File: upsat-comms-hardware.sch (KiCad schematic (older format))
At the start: 195 parts, among them J1 SMA, J2 SMA, P1 SWD, P2 OBC, P3 CONN_02X03, U1 TXCO_TG_5021CG, U10 CC1120, U12 ADT7420, U14 OPA320, U16 RF5110G, U18 FA_128_, U2 TPS79930, U3 FA_128_, U4 CC1120, U5 STM32F407VG, U6 TXCO_TG_5021CG, U8 TPS79930, Y1 Crystal, Y2 Crystal

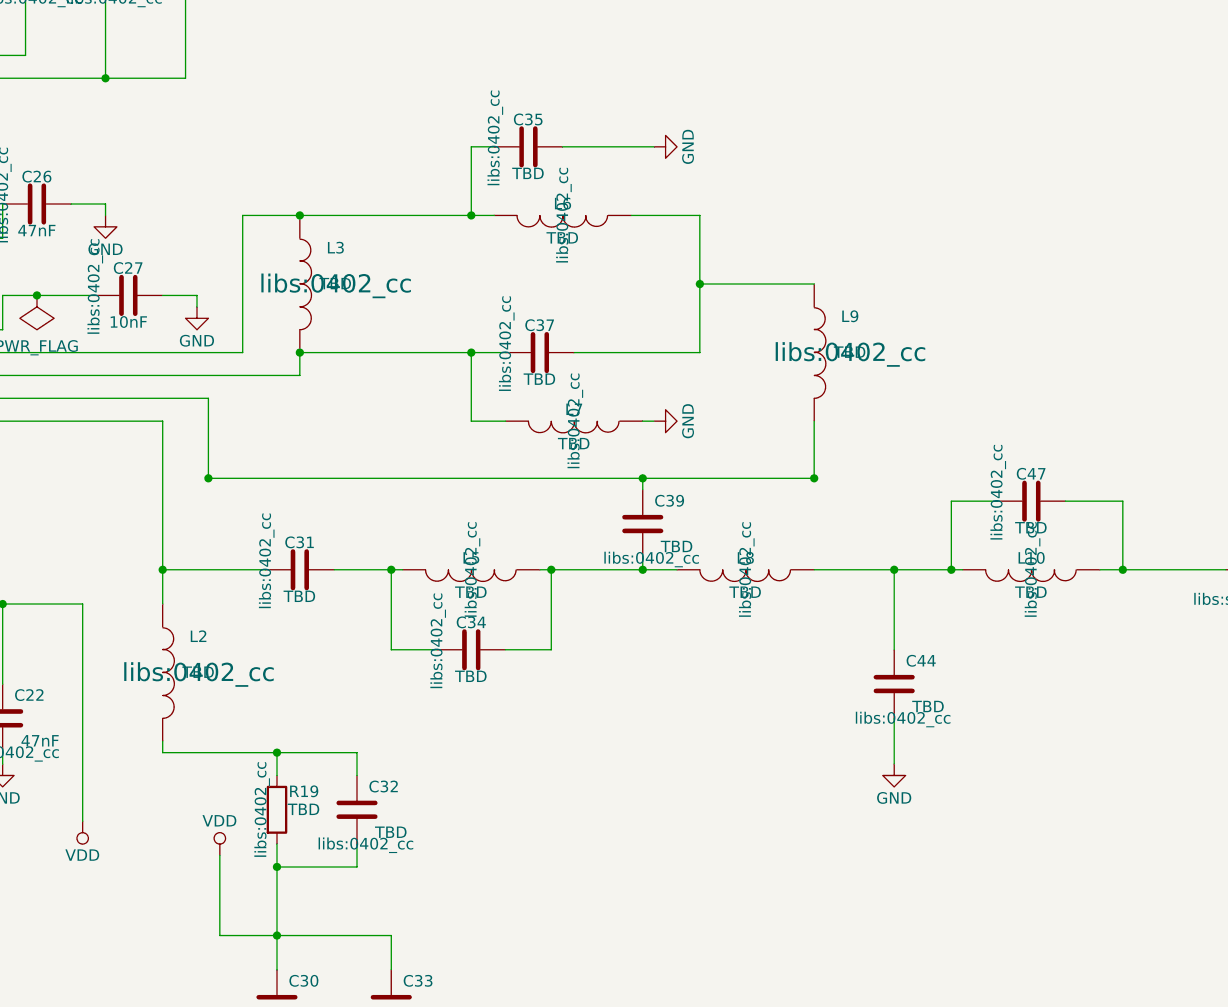
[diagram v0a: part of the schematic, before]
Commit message: add RF values for CC1120 RX, wrong path for mmcx con.
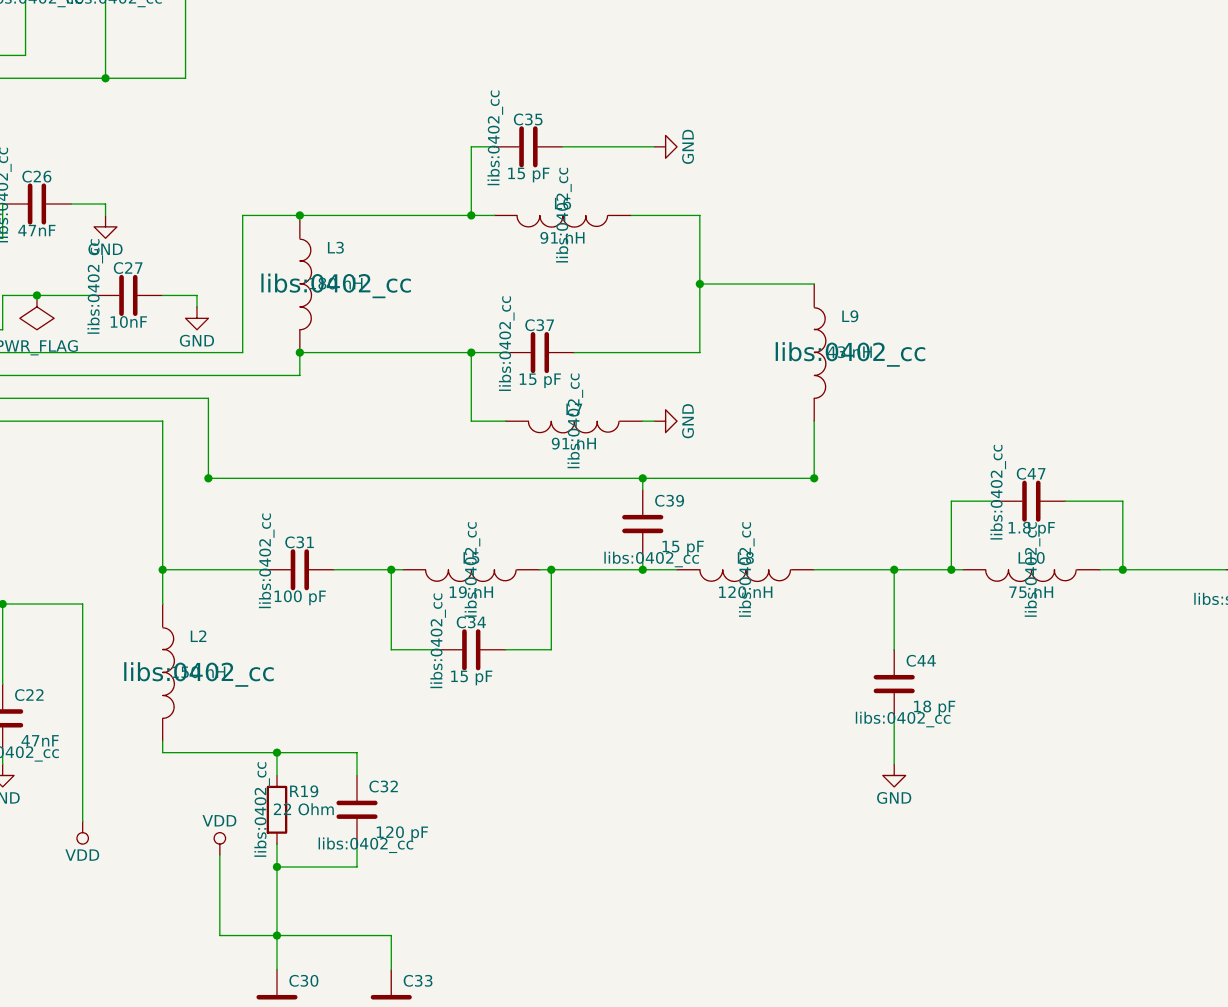
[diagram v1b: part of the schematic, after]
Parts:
- C31: value TBD -> 100 pF
- C32: value TBD -> 120 pF
- C34, C35, C37, C39: value TBD -> 15 pF
- C44: value TBD -> 18 pF
- C47: value TBD -> 1.8 pF
- L10: value TBD -> 75 nH
- L2: value TBD -> 150 nH
- L3: value TBD -> 180 nH
- L5: value TBD -> 19 nH
- L6, L7: value TBD -> 91 nH
- L8: value TBD -> 120 nH
- L9: value TBD -> 43 nH
- R19: value TBD -> 22 Ohm
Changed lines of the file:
@@
 P 6350 16800
 F 0 "L2" H 6507 16957 50  0000 C CNN
-F 1 "TBD" H 6507 16800 50  0000 C CNN
+F 1 "150 nH" H 6507 16800 50  0000 C CNN
 F 2 "libs:0402_cc" H 6507 16800 79  0000 C CNN
 F 3 "" H 6350 16800 50  0000 C CNN
@@
 P 6850 17400
 F 0 "R19" H 6968 17479 50  0000 C CNN
-F 1 "TBD" H 6968 17400 50  0000 C CNN
+F 1 "22 Ohm" H 6968 17400 50  0000 C CNN
 F 2 "libs:0402_cc" V 6780 17400 50  0000 C CNN
 F 3 "" H 6850 17400 50  0000 C CNN
@@
 P 7200 17400
 F 0 "C32" H 7318 17500 50  0000 C CNN
-F 1 "TBD" H 7279 17300 50  0000 L CNN
+F 1 "120 pF" H 7279 17300 50  0000 L CNN
 F 2 "libs:0402_cc" H 7238 17250 50  0000 C CNN
 F 3 "" H 7200 17400 50  0000 C CNN
@@
 P 6950 16350
 F 0 "C31" V 7068 16350 50  0000 C CNN
-F 1 "TBD" V 6832 16350 50  0000 C CNN
+F 1 "100 pF" V 6832 16350 50  0000 C CNN
 F 2 "libs:0402_cc" H 6988 16200 50  0000 C CNN
 F 3 "" H 6950 16350 50  0000 C CNN
@@
 P 7700 16350
 F 0 "L5" V 7650 16350 50  0000 C CNN
-F 1 "TBD" V 7800 16350 50  0000 C CNN
+F 1 "19 nH" V 7800 16350 50  0000 C CNN
 F 2 "libs:0402_cc" H 7700 16350 50  0000 C CNN
 F 3 "" H 7700 16350 50  0000 C CNN
@@
 P 7700 16700
 F 0 "C34" V 7818 16700 50  0000 C CNN
-F 1 "TBD" V 7582 16700 50  0000 C CNN
+F 1 "15 pF" V 7582 16700 50  0000 C CNN
 F 2 "libs:0402_cc" H 7738 16550 50  0000 C CNN
 F 3 "" H 7700 16700 50  0000 C CNN
@@
 P 8450 16150
 F 0 "C39" H 8568 16250 50  0000 C CNN
-F 1 "TBD" H 8529 16050 50  0000 L CNN
+F 1 "15 pF" H 8529 16050 50  0000 L CNN
 F 2 "libs:0402_cc" H 8488 16000 50  0000 C CNN
 F 3 "" H 8450 16150 50  0000 C CNN
@@
 P 6950 15100
 F 0 "L3" H 7107 15257 50  0000 C CNN
-F 1 "TBD" H 7107 15100 50  0000 C CNN
+F 1 "180 nH" H 7107 15100 50  0000 C CNN
 F 2 "libs:0402_cc" H 7107 15100 79  0000 C CNN
 F 3 "" H 6950 15100 50  0000 C CNN
@@
 P 8150 15700
 F 0 "L7" V 8100 15700 50  0000 C CNN
-F 1 "TBD" V 8250 15700 50  0000 C CNN
+F 1 "91 nH" V 8250 15700 50  0000 C CNN
 F 2 "libs:0402_cc" H 8150 15700 50  0000 C CNN
 F 3 "" H 8150 15700 50  0000 C CNN
@@
 P 8100 14800
 F 0 "L6" V 8050 14800 50  0000 C CNN
-F 1 "TBD" V 8200 14800 50  0000 C CNN
+F 1 "91 nH" V 8200 14800 50  0000 C CNN
 F 2 "libs:0402_cc" H 8100 14800 50  0000 C CNN
 F 3 "" H 8100 14800 50  0000 C CNN
@@
 P 8000 15400
 F 0 "C37" V 8118 15400 50  0000 C CNN
-F 1 "TBD" V 7882 15400 50  0000 C CNN
+F 1 "15 pF" V 7882 15400 50  0000 C CNN
 F 2 "libs:0402_cc" H 8038 15250 50  0000 C CNN
 F 3 "" H 8000 15400 50  0000 C CNN
@@
 P 7950 14500
 F 0 "C35" V 8068 14500 50  0000 C CNN
-F 1 "TBD" V 7832 14500 50  0000 C CNN
+F 1 "15 pF" V 7832 14500 50  0000 C CNN
 F 2 "libs:0402_cc" H 7988 14350 50  0000 C CNN
 F 3 "" H 7950 14500 50  0000 C CNN
@@
 P 9200 15400
 F 0 "L9" H 9357 15557 50  0000 C CNN
-F 1 "TBD" H 9357 15400 50  0000 C CNN
+F 1 "43 nH" H 9357 15400 50  0000 C CNN
 F 2 "libs:0402_cc" H 9357 15400 79  0000 C CNN
 F 3 "" H 9200 15400 50  0000 C CNN
@@
 P 8900 16350
 F 0 "L8" V 8850 16350 50  0000 C CNN
-F 1 "TBD" V 9000 16350 50  0000 C CNN
+F 1 "120 nH" V 9000 16350 50  0000 C CNN
 F 2 "libs:0402_cc" H 8900 16350 50  0000 C CNN
 F 3 "" H 8900 16350 50  0000 C CNN
@@
 P 9550 16850
 F 0 "C44" H 9668 16950 50  0000 C CNN
-F 1 "TBD" H 9629 16750 50  0000 L CNN
+F 1 "18 pF" H 9629 16750 50  0000 L CNN
 F 2 "libs:0402_cc" H 9588 16700 50  0000 C CNN
 F 3 "" H 9550 16850 50  0000 C CNN
@@
 P 10150 16350
 F 0 "L10" V 10100 16350 50  0000 C CNN
-F 1 "TBD" V 10250 16350 50  0000 C CNN
+F 1 "75 nH" V 10250 16350 50  0000 C CNN
 F 2 "libs:0402_cc" H 10150 16350 50  0000 C CNN
 F 3 "" H 10150 16350 50  0000 C CNN
@@
 P 10150 16050
 F 0 "C47" V 10268 16050 50  0000 C CNN
-F 1 "TBD" V 10032 16050 50  0000 C CNN
+F 1 "1.8 pF" V 10032 16050 50  0000 C CNN
 F 2 "libs:0402_cc" H 10188 15900 50  0000 C CNN
 F 3 "" H 10150 16050 50  0000 C CNN

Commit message: add power amp RF out component values, add comments on CC1120 TXCO-Crystal section, add comments on CC1120 regulator-bead
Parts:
- C160: value 22-30pF -> 22 pF
- C31: value 100 pF -> 150 pF
- C32: value 120 pF -> 100 pF
- L33: value 2.7-3.9nH -> 2.7 nH
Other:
- note added: "CC1120/25 uning XTAL: do not mount: U1, C3, C9, R9, R6\nCC1120/25 using TCXO: do not mount: R10, R9, C10, U3, C11: mount 0 Ohm resisitor\n X1: CC1120:32MHz and CC1125:40MHz\n R10 is a 0ohms shunt resistor that ground\n the EXT_XOSC pin when TCXO is not mounted.\n"
- note added: "CC1120/25 uning XTAL: do not mount: U6, C53, C65, R26, R24\nCC1120/25 using TCXO: do not mount: R27, R26, C67, U18, C69: mount 0 Ohm resistor\n X1: CC1120:32MHz and CC1125:40MHz\n R27 is a 0ohms shunt resistor that ground\n the EXT_XOSC pin when TCXO is not mounted.\n"
- note added: "L1 is a Bead to be mounted if the regulator U2 is not mounted,\nCC1120 ref des will default not use regulator\nCC1120/CC1125: do not mount: U2, C4, C8, C13\nTG5021CG is optional: do not mount L1 if regulator is mounted\n"
- note added: "L11 is a Bead to be mounted if the regulator U8 is not mounted,\nCC1120 ref des will default not use regulator\nCC1120/CC1125: do not mount: U8, C55, C62, C73\nTG5021CG is optional: do not mount L1 if regulator is mounted\n"
- note removed: "CC1120/25 uning XTAL: do not mount: X2, C321, C322, R321, R322\nCC1120/25 using TCXO: do not mount: R12, R321, C311, X1. C301: mount 0 Ohm resisitor\n X1: CC1120:32MHz and CC1125:40MHz\n R12 is a 0ohms shunt resistor that ground\n the EXT_XOSC pin when TCXO is not mounted.\n"
- note removed: "L1 is a Bead to be mounted if the regulator U2 is not mounted,\nCC1120 ref des will default not use regulator\nCC1120/CC1125: do not mount: U2, C12, C41, C53\nTG5021CG is optional: do not mount L1 if regulator is mounted\n"
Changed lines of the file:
@@
 $EndComp
 Text Notes 1600 18350 0    60   ~ 0
-L1 is a Bead to be mounted if the regulator U2 is not mounted,\nCC1120 ref des will default not use regulator\nCC1120/CC1125: do not mount: U2, C12, C41, C53\nTG5021CG is optional: do not mount L1 if regulator is mounted\n
+L1 is a Bead to be mounted if the regulator U2 is not mounted,\nCC1120 ref des will default not use regulator\nCC1120/CC1125: do not mount: U2, C4, C8, C13\nTG5021CG is optional: do not mount L1 if regulator is mounted\n
 $Comp
 L R R17
@@
 P 7200 17400
 F 0 "C32" H 7318 17500 50  0000 C CNN
-F 1 "120 pF" H 7279 17300 50  0000 L CNN
+F 1 "100 pF" H 7279 17300 50  0000 L CNN
 F 2 "libs:0402_cc" H 7238 17250 50  0000 C CNN
 F 3 "" H 7200 17400 50  0000 C CNN
@@
 P 6950 16350
 F 0 "C31" V 7068 16350 50  0000 C CNN
-F 1 "100 pF" V 6832 16350 50  0000 C CNN
+F 1 "150 pF" V 6832 16350 50  0000 C CNN
 F 2 "libs:0402_cc" H 6988 16200 50  0000 C CNN
 F 3 "" H 6950 16350 50  0000 C CNN
@@
 $EndComp
 Text Notes 1600 12150 0    60   ~ 0
-CC1120/25 uning XTAL: do not mount: X2, C321, C322, R321, R322\nCC1120/25 using TCXO: do not mount: R12, R321, C311, X1. C301: mount 0 Ohm resisitor\n X1: CC1120:32MHz and CC1125:40MHz\n R12 is a 0ohms shunt resistor that ground\n the EXT_XOSC pin when TCXO is not mounted.\n
+CC1120/25 uning XTAL: do not mount: U1, C3, C9, R9, R6\nCC1120/25 using TCXO: do not mount: R10, R9, C10, U3, C11: mount 0 Ohm resisitor\n X1: CC1120:32MHz and CC1125:40MHz\n R10 is a 0ohms shunt resistor that ground\n the EXT_XOSC pin when TCXO is not mounted.\n
 $Comp
 L SMA J1
@@
 P 28300 16150
 F 0 "L33" V 28250 16150 50  0000 C CNN
-F 1 "2.7-3.9nH" V 28400 16150 50  0000 C CNN
+F 1 "2.7 nH" V 28400 16150 50  0000 C CNN
 F 2 "libs:0603murata2" H 28300 16150 50  0000 C CNN
 F 3 "" H 28300 16150 50  0000 C CNN
@@
 P 28900 16550
 F 0 "C160" H 29018 16650 50  0000 C CNN
-F 1 "22-30pF" H 28979 16450 50  0000 L CNN
+F 1 "22 pF" H 28979 16450 50  0000 L CNN
 F 2 "libs:0603murata2" H 28938 16400 50  0000 C CNN
 F 3 "" H 28900 16550 50  0000 C CNN
@@
 $EndComp
 Text Notes 14350 12050 0    60   ~ 0
-CC1120/25 uning XTAL: do not mount: X2, C321, C322, R321, R322\nCC1120/25 using TCXO: do not mount: R12, R321, C311, X1. C301: mount 0 Ohm resisitor\n X1: CC1120:32MHz and CC1125:40MHz\n R12 is a 0ohms shunt resistor that ground\n the EXT_XOSC pin when TCXO is not mounted.\n
+CC1120/25 uning XTAL: do not mount: U6, C53, C65, R26, R24\nCC1120/25 using TCXO: do not mount: R27, R26, C67, U18, C69: mount 0 Ohm resistor\n X1: CC1120:32MHz and CC1125:40MHz\n R27 is a 0ohms shunt resistor that ground\n the EXT_XOSC pin when TCXO is not mounted.\n
 $Comp
 L C C139
@@
 $EndComp
 Text Notes 14350 18250 0    60   ~ 0
-L1 is a Bead to be mounted if the regulator U2 is not mounted,\nCC1120 ref des will default not use regulator\nCC1120/CC1125: do not mount: U2, C12, C41, C53\nTG5021CG is optional: do not mount L1 if regulator is mounted\n
+L11 is a Bead to be mounted if the regulator U8 is not mounted,\nCC1120 ref des will default not use regulator\nCC1120/CC1125: do not mount: U8, C55, C62, C73\nTG5021CG is optional: do not mount L1 if regulator is mounted\n
 $Comp
 L +3.3V #PWR0118

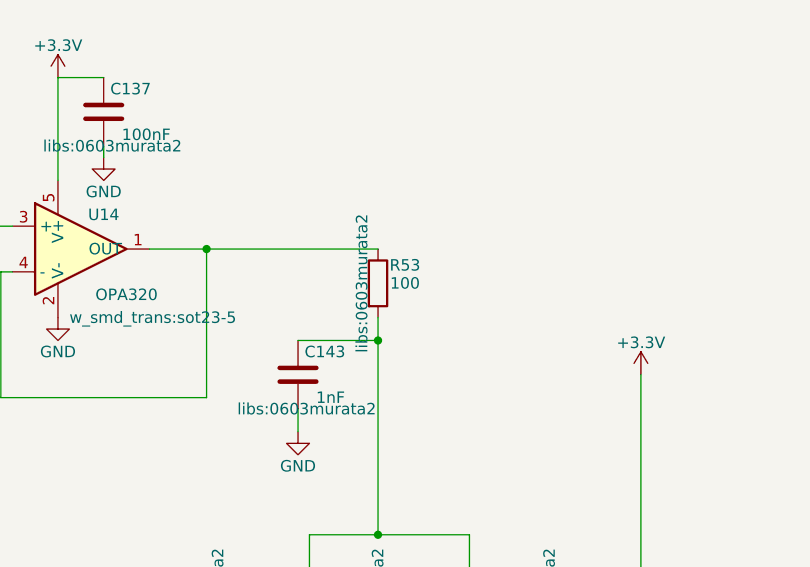
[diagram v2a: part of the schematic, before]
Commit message: Edit OPA R53 resistor
It should be 180 Ohms to feed P.A AGC with 2.75 Volts.
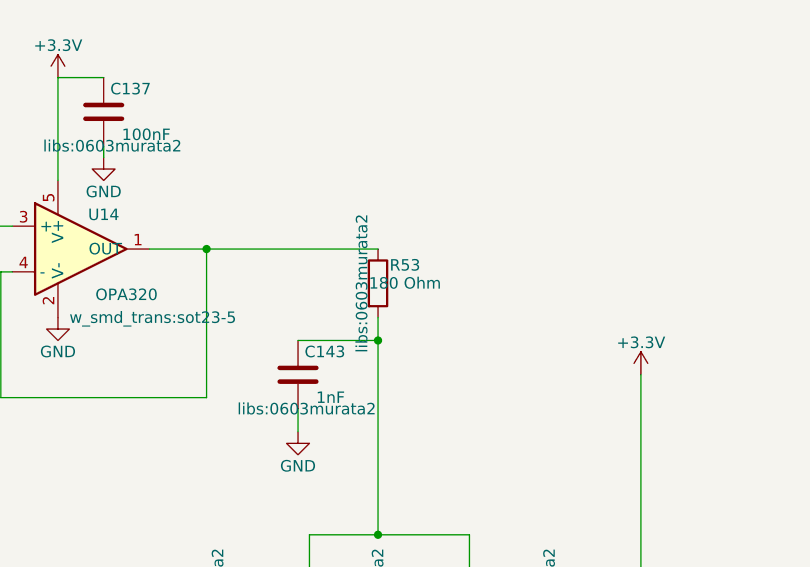
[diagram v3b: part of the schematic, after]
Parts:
- R53: value 100 -> 180 Ohm
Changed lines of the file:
@@
 P 26200 13350
 F 0 "R53" H 26318 13429 50  0000 C CNN
-F 1 "100" H 26318 13350 50  0000 C CNN
+F 1 "180 Ohm" H 26318 13350 50  0000 C CNN
 F 2 "libs:0603murata2" V 26130 13350 50  0000 C CNN
 F 3 "" H 26200 13350 50  0000 C CNN

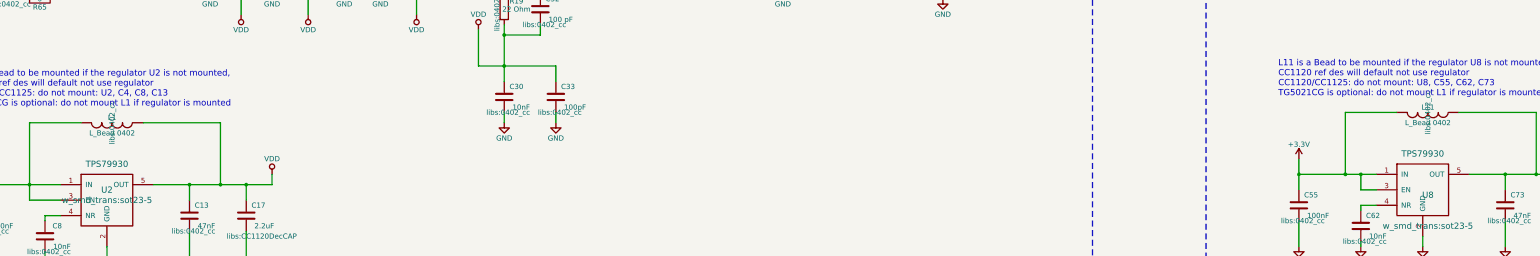
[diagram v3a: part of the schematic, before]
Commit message: Add CC1120 bead part number
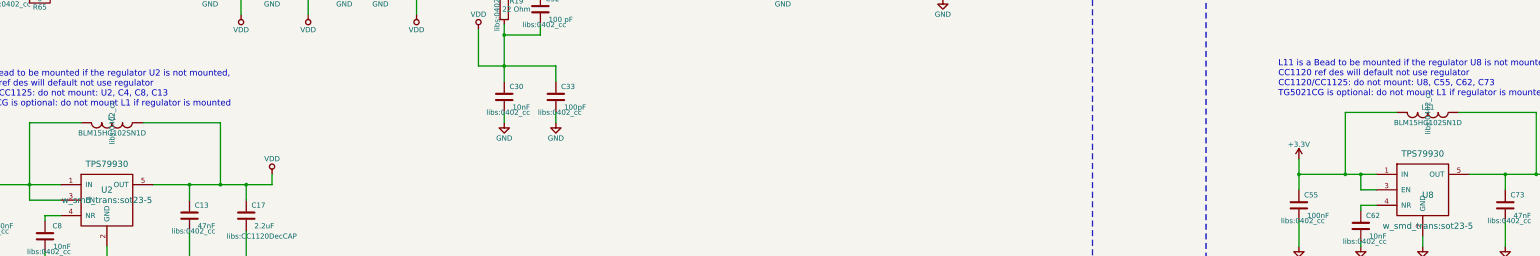
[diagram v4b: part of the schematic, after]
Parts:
- L1, L11: value L_Bead 0402 -> BLM15HG102SN1D
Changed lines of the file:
@@
 P 3050 18500
 F 0 "L1" V 3000 18500 50  0000 C CNN
-F 1 "L_Bead 0402" V 3150 18500 50  0000 C CNN
+F 1 "BLM15HG102SN1D" V 3150 18500 50  0000 C CNN
 F 2 "libs:0402_cc" H 3050 18500 50  0000 C CNN
 F 3 "" H 3050 18500 50  0000 C CNN
@@
 P 15800 18400
 F 0 "L11" V 15750 18400 50  0000 C CNN
-F 1 "L_Bead 0402" V 15900 18400 50  0000 C CNN
+F 1 "BLM15HG102SN1D" V 15900 18400 50  0000 C CNN
 F 2 "libs:0402_cc" H 15800 18400 50  0000 C CNN
 F 3 "" H 15800 18400 50  0000 C CNN

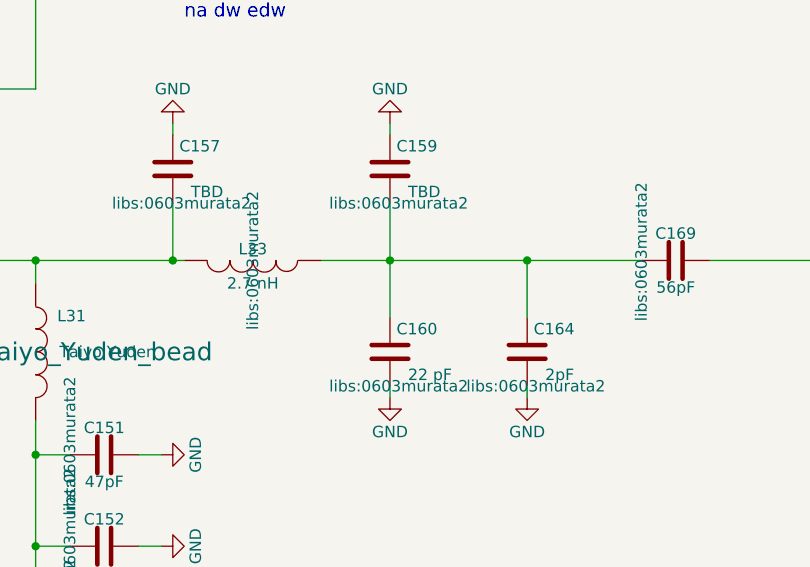
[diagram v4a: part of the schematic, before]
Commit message: Add values for P.A RF Out matching network
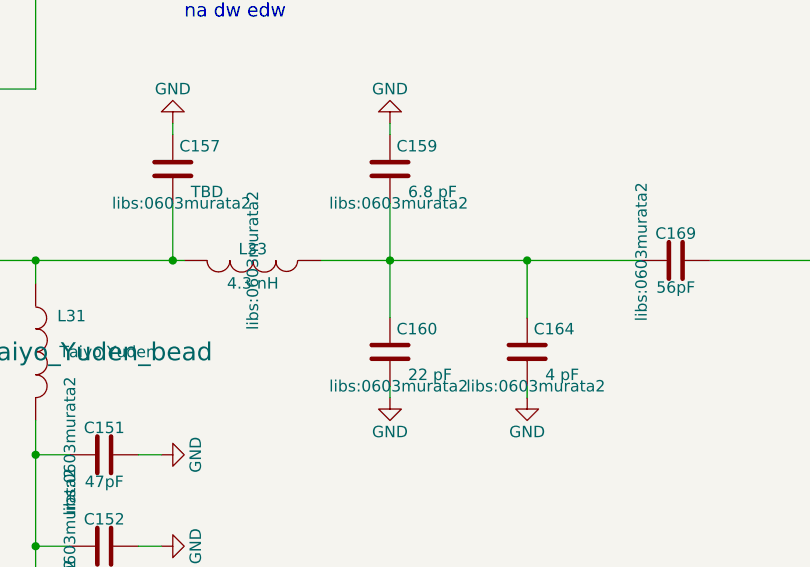
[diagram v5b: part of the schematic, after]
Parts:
- C159: value TBD -> 6.8 pF
- C164: value 2pF -> 4 pF
- L33: value 2.7 nH -> 4.3 nH
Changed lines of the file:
@@
 P 28300 16150
 F 0 "L33" V 28250 16150 50  0000 C CNN
-F 1 "2.7 nH" V 28400 16150 50  0000 C CNN
+F 1 "4.3 nH" V 28400 16150 50  0000 C CNN
 F 2 "libs:0603murata2" H 28300 16150 50  0000 C CNN
 F 3 "" H 28300 16150 50  0000 C CNN
@@
 P 29500 16550
 F 0 "C164" H 29618 16650 50  0000 C CNN
-F 1 "2pF" H 29579 16450 50  0000 L CNN
+F 1 "4 pF" H 29579 16450 50  0000 L CNN
 F 2 "libs:0603murata2" H 29538 16400 50  0000 C CNN
 F 3 "" H 29500 16550 50  0000 C CNN
@@
 P 28900 15750
 F 0 "C159" H 29018 15850 50  0000 C CNN
-F 1 "TBD" H 28979 15650 50  0000 L CNN
+F 1 "6.8 pF" H 28979 15650 50  0000 L CNN
 F 2 "libs:0603murata2" H 28938 15600 50  0000 C CNN
 F 3 "" H 28900 15750 50  0000 C CNN
